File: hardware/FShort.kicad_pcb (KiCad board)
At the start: 2 copper layers, 76.8 x 60.4 mm, 47 parts, among them J1 Conn_01x03_Male, J10 Conn_01x04_Male, J11 Conn_02x05_Odd_Even, J12 Conn_02x03_Odd_Even, J13 MicroSD, J14 Conn_01x01_Male, J2 Conn_01x07_Female, J3 Conn_01x03_Male, J4 Conn_01x03_Male, J5 USB_B_Micro, J6 Conn_02x05_Odd_Even, J7 Conn_01x04_Male, J8 Conn_01x04_Male, J9 Conn_01x04_Male, SW1 SW_Push, U1 STM32F103RETx, U2 SN74LVC1T45DBV, U3 SN74LVC1T45DBV, U4 AP7365-SOT25, U5 W25Q64JV, U6 E19-868M30S, Y1 8Mhz, Y2 32.768KHz

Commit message: New version of PCB, several bugs fixed
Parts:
- removed J14: Conn_01x01_Male, Connector_Wire:SolderWirePad_1x01_SMD_5x10mm
- removed MH1, MH2: MountingHole_2.2mm_M2_Pad_Via, MountingHole:MountingHole_2.2mm_M2_Pad_Via
- added AE1: Antenna_Shield, Personal:KH-IPEX3-2020, F.Cu at (104.1, 82.4)
- added C15: 3n3, Capacitor_SMD:C_0603_1608Metric, F.Cu at (160.8, 90.9)
- added C16: 3n3, Capacitor_SMD:C_0603_1608Metric, F.Cu at (165.3, 82.8)
- added D2: ZMM7V5, Diode_SMD:D_MiniMELF, F.Cu at (165.1, 93.8)
- added D3: ZMM7V5, Diode_SMD:D_MiniMELF, F.Cu at (164.2, 84.9)
- added E1: SPARK_GAP, Personal:SDI12-SparkGap, F.Cu at (168.4, 94.9)
- added E2: SPARK_GAP, Personal:SDI12-SparkGap, F.Cu at (170.4, 70.3)
- added R10: 510, Resistor_SMD:R_0603_1608Metric, F.Cu at (162.8, 90.9)
- added R11: 200k, Resistor_SMD:R_0603_1608Metric, F.Cu at (165.3, 81.1)
- added R12: 510, Resistor_SMD:R_0603_1608Metric, F.Cu at (168.1, 83.9)
- added R7: 510, Resistor_SMD:R_0603_1608Metric, F.Cu at (162.8, 94.2)
- added R8: 200k, Resistor_SMD:R_0603_1608Metric, F.Cu at (160.8, 94.2)
- added R9: 510, Resistor_SMD:R_0603_1608Metric, F.Cu at (169.3, 80.4)
- U5: footprint Package_SO:SOP-8_3.9x4.9mm_P1.27mm -> Package_SO:SOP-8_5.28x5.23mm_P1.27mm
- U6: value E19-868M30S -> E19-868M30S_Vollgo; footprint Personal:E19-868MS1W -> Personal:E19-868MS1W_VollGo
- moved U6 2.06 mm to (127.8, 76.4)
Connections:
- J3 pad 2: Net-(J3-Pad2) -> Net-(E1-Pad1)
- J4 pad 2: Net-(J4-Pad2) -> Net-(E2-Pad1)
- U2 pad 3: Net-(J3-Pad2) -> Net-(R10-Pad2)
- U3 pad 3: Net-(J4-Pad2) -> Net-(R12-Pad1)
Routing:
- net GND: track 466.2 -> 522.3 mm
- net Net-(U6-Pad5): track 0.00 -> 25.1 mm, vias 0 -> 2
- net RADIO_NSS: track 18.7 -> 41.3 mm, vias 0 -> 3
- net Radio_rst: track 44.6 -> 66.9 mm, vias 2 -> 4
- net Net-(U6-Pad3): track 0.00 -> 21.9 mm
- net +5V: track 145.6 -> 166.5 mm
- net Net-(U6-Pad4): track 0.00 -> 18.6 mm
- net Net-(E2-Pad1): track 0.00 -> 13.3 mm
- net Net-(E1-Pad1): track 0.00 -> 13.0 mm
- net Net-(U6-Pad2): track 0.00 -> 11.2 mm
- net Net-(AE1-Pad1): track 0.00 -> 9.60 mm
- net Net-(C16-Pad1): track 0.00 -> 8.94 mm
- net Net-(C15-Pad1): track 0.00 -> 8.87 mm
- net Net-(J4-Pad2): track 8.84 -> 0.00 mm, vias 1 -> 0
- net Net-(J14-Pad1): track 8.68 -> 0.00 mm, vias 1 -> 0
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
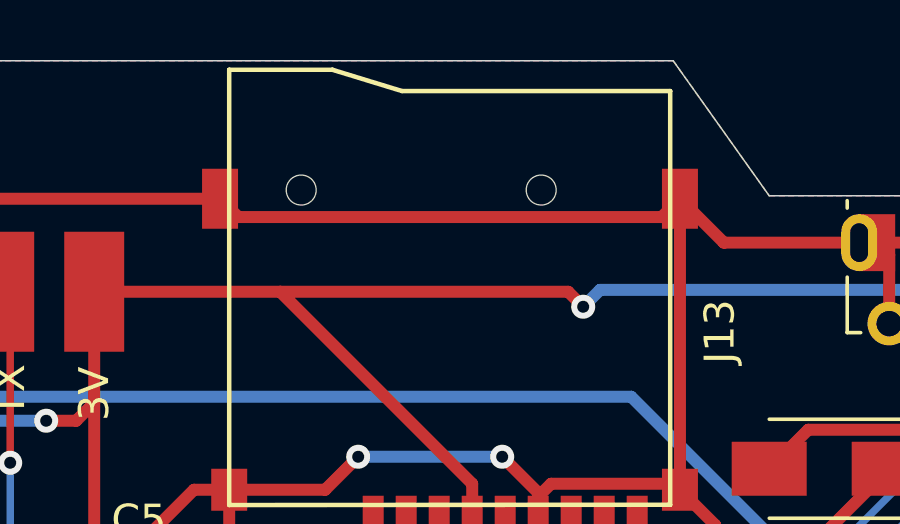
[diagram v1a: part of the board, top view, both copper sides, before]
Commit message: First fully working version.
Improved file system to allow more columns in tables.
Added a vector class to mem_structs.
Added memory move capabilities to some memory structs.
Fully working SDI12 driver.
Updated PCB.
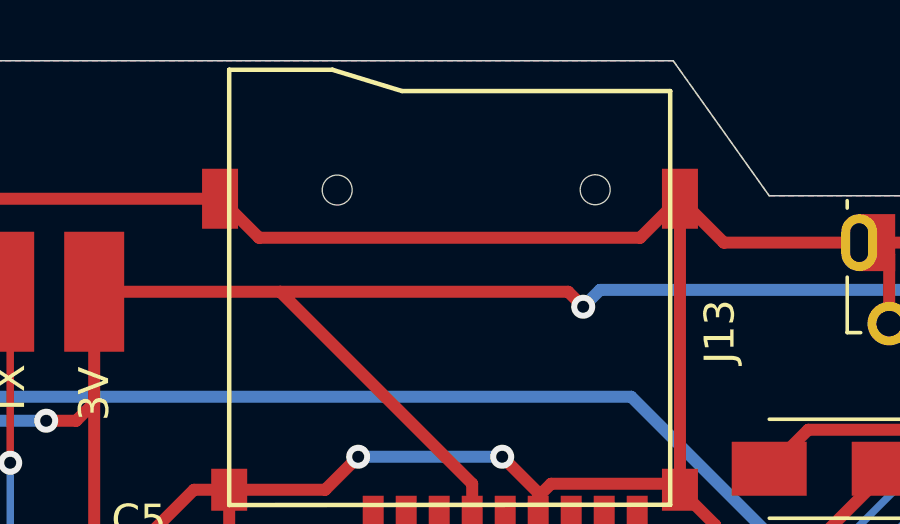
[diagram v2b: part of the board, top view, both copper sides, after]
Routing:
- net GND: track 522.3 -> 522.8 mm

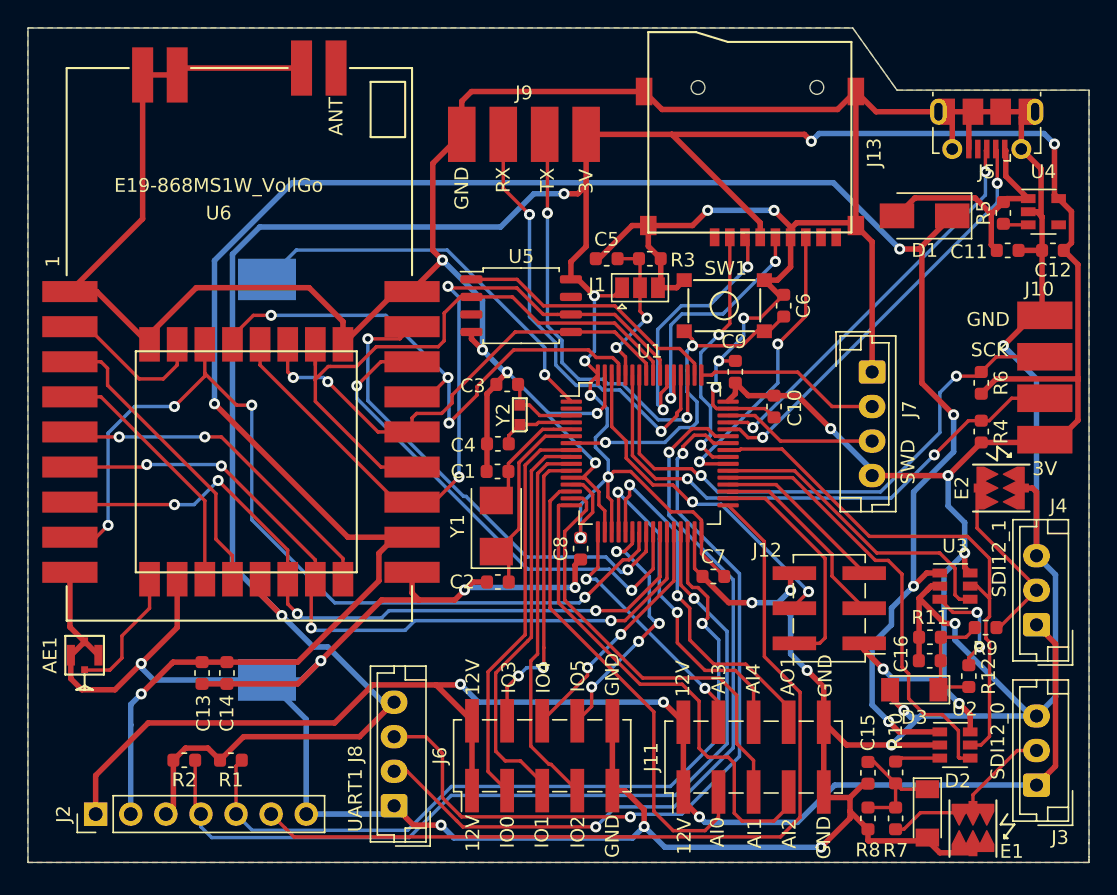
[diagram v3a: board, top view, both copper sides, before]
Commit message: Added USB support Added Port and Socket abstraction classes Added simple HTTP support through GSM Added a kernel level message queue
KVS module setting system
LoRa variable refactoring
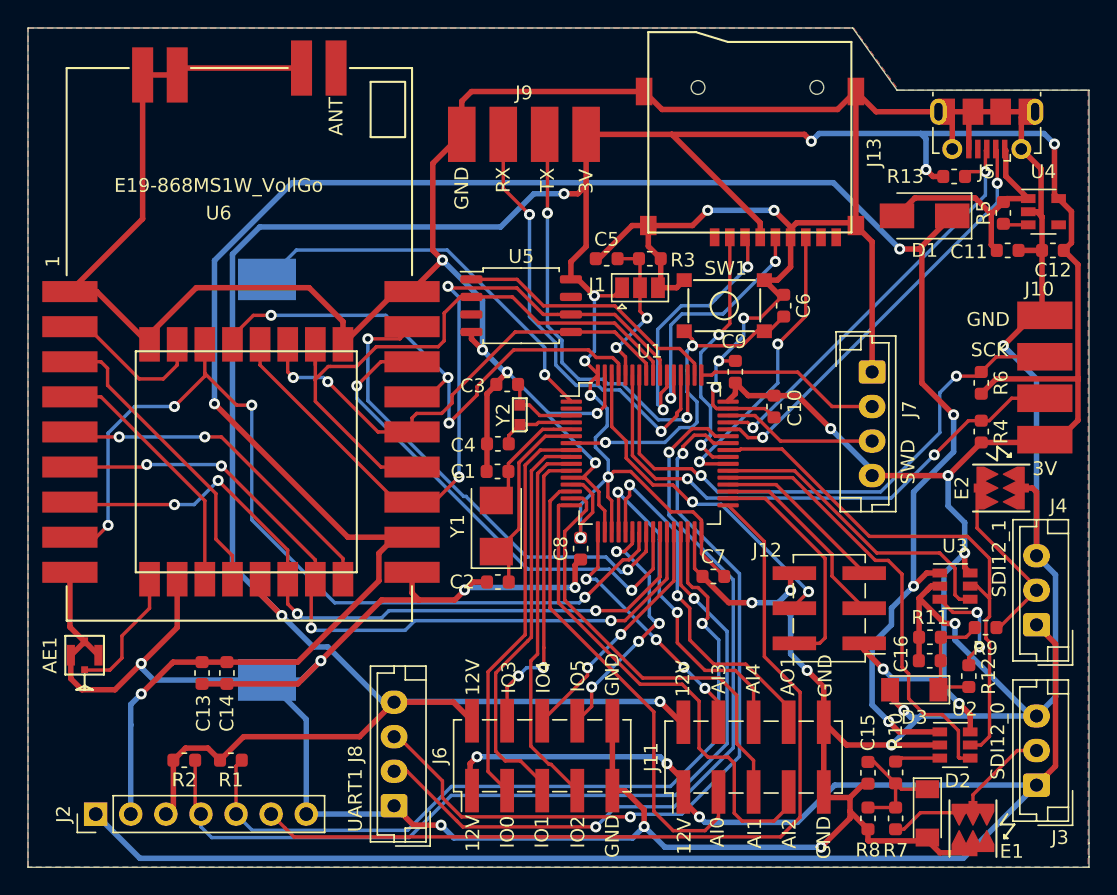
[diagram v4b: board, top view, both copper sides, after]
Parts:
- added R13: 1k5, Resistor_SMD:R_0603_1608Metric, F.Cu at (167.0, 47.8)
- C3, C4: value 20p -> 15p
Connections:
- J11 pad 2: +12V -> +3V3
- J6 pad 2: +12V -> +3V3
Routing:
- net +3V3: track 284.0 -> 316.1 mm, vias 14 -> 16
- net +12V: track 103.7 -> 131.5 mm
- net USB_DP: track 29.1 -> 30.8 mm
- net UART1_TX: track 59.4 -> 58.2 mm
- net ADC3: vias 2 -> 4
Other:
- board size 76.8 x 60.4 mm -> 76.8 x 60.8 mm
